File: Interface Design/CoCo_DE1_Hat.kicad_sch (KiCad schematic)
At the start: 24 parts, among them J1 J1, J2 J2, J3 J3, J4 J4, J5 J5, J6 J6, U1 74LVC245A, U2 74LVC245A, U3 74LVC245A, U4 74LVC245A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

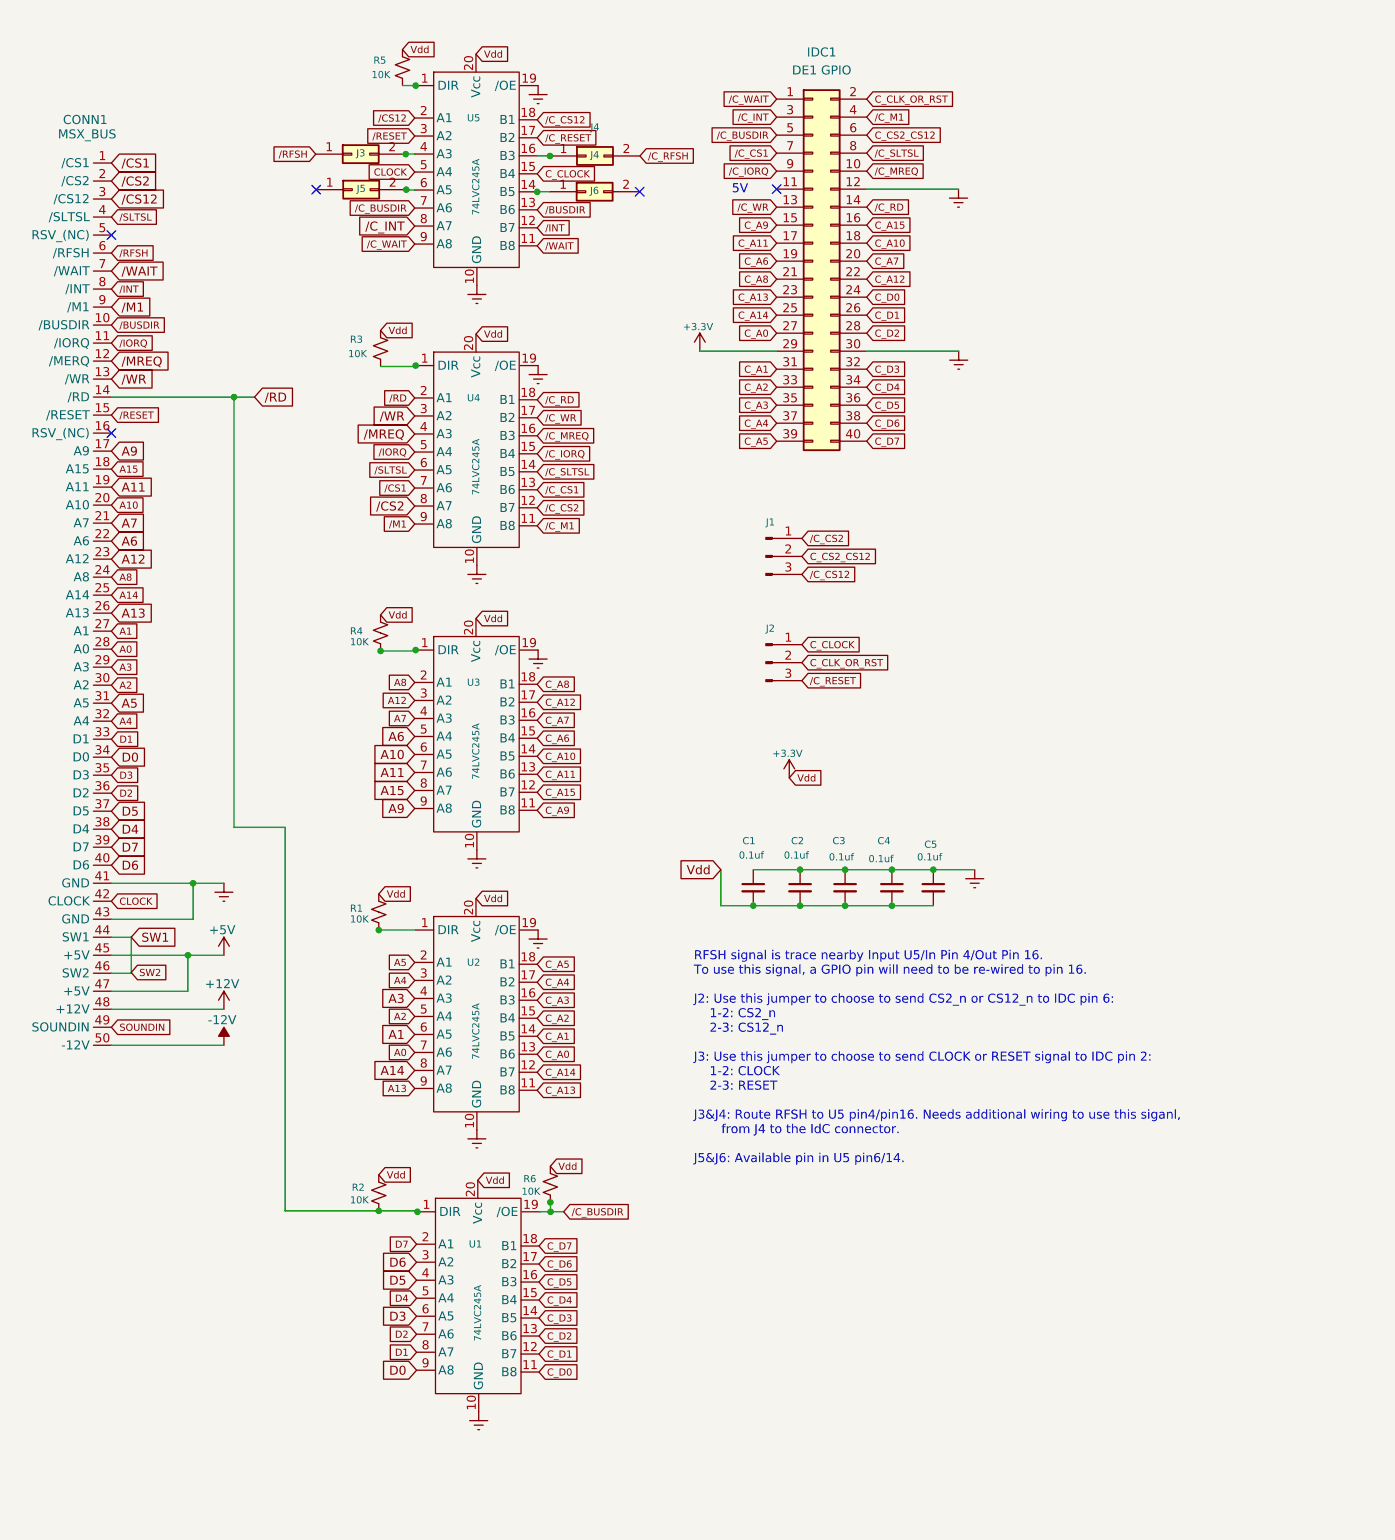
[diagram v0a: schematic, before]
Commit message: Adding PCB layout
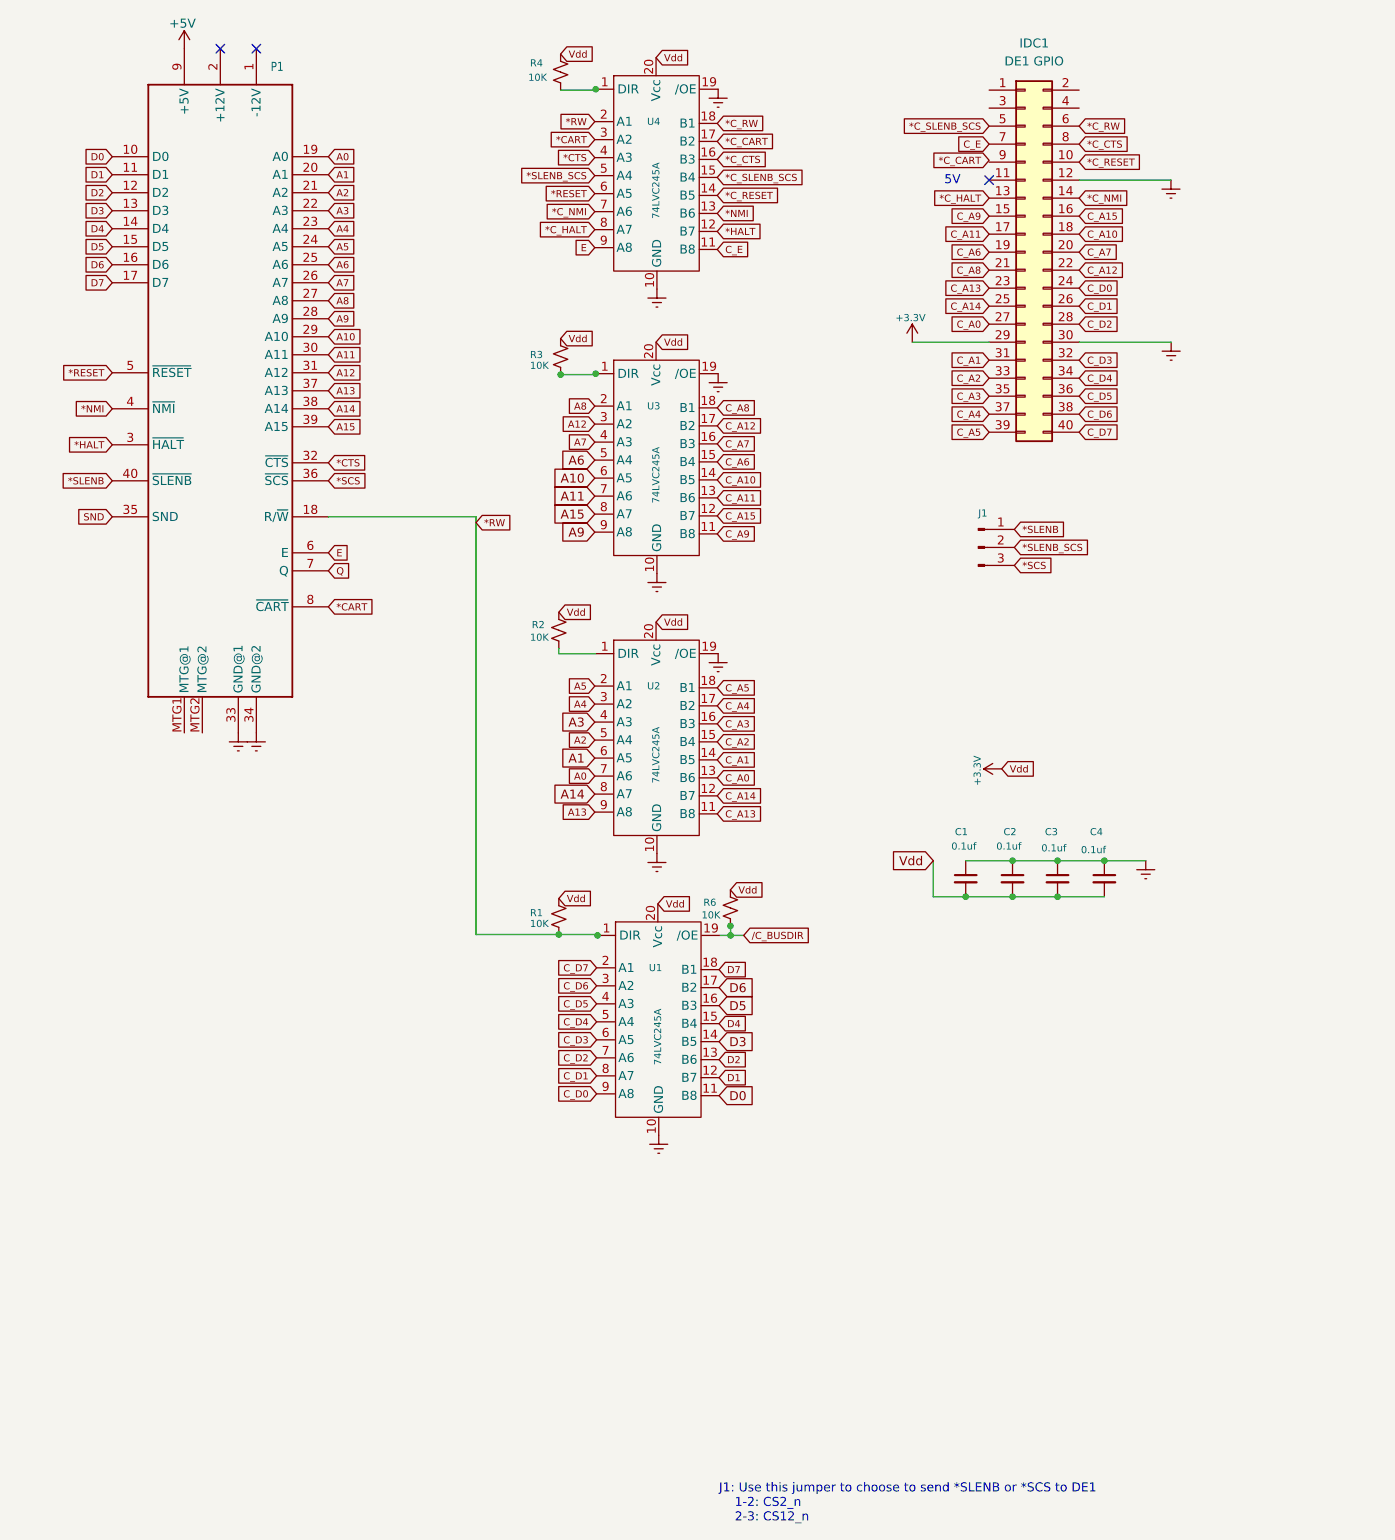
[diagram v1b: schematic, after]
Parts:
- removed C5: 0.1uf, Capacitor_THT:C_Disc_D3.0mm_W1.6mm_P2.50mm, symbol Device:C_Small
- removed CONN1: MSX_BUS, Roni Footprints:MSX_CART, symbol Roni:MSX_BUS
- removed J2: J2, Connector_PinHeader_2.54mm:PinHeader_1x03_P2.54mm_Vertical, symbol Connector:Conn_01x03_Male
- removed J3: J3, Connector_PinHeader_2.54mm:PinHeader_1x02_P2.54mm_Vertical, symbol Connector_Generic:Conn_02x01
- removed J4: J4, Connector_PinHeader_2.54mm:PinHeader_1x02_P2.54mm_Vertical, symbol Connector_Generic:Conn_02x01
- removed J5: J5, Connector_PinHeader_2.54mm:PinHeader_1x02_P2.54mm_Vertical, symbol Connector_Generic:Conn_02x01
- removed J6: J6, Connector_PinHeader_2.54mm:PinHeader_1x02_P2.54mm_Vertical, symbol Connector_Generic:Conn_02x01
- removed R5: 10K, Resistor_THT:R_Axial_DIN0207_L6.3mm_D2.5mm_P7.62mm_Horizontal, symbol Device:R_Small_US
- removed U5: 74LVC245A, Package_DIP:DIP-20_W7.62mm, symbol Roni:74LVC245A
- added P1: CoCo_Slot, Roni Footprints:COCO-CART-HAT, symbol Roni Symbols:CoCo_Slot
- IDC1: footprint Connector_IDC:IDC-Header_2x20_P2.54mm_Vertical -> Connector_PinHeader_2.54mm:PinHeader_2x20_P2.54mm_Vertical
- R1, R2, R6: footprint Resistor_THT:R_Axial_DIN0207_L6.3mm_D2.5mm_P7.62mm_Horizontal -> Resistor_THT:R_Axial_DIN0204_L3.6mm_D1.6mm_P5.08mm_Horizontal
- R3: renamed from R4; footprint Resistor_THT:R_Axial_DIN0207_L6.3mm_D2.5mm_P7.62mm_Horizontal -> Resistor_THT:R_Axial_DIN0204_L3.6mm_D1.6mm_P5.08mm_Horizontal
- R4: renamed from R3; footprint Resistor_THT:R_Axial_DIN0207_L6.3mm_D2.5mm_P7.62mm_Horizontal -> Resistor_THT:R_Axial_DIN0204_L3.6mm_D1.6mm_P5.08mm_Horizontal
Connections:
- net +5V: now also P1.9 (+5V)
- net A0: now also P1.19 (A0)
- net A1: now also P1.20 (A1)
- net A10: now also P1.29 (A10)
- net A11: now also P1.30 (A11)
- net A12: now also P1.31 (A12)
- net A13: now also P1.37 (A13)
- net A14: now also P1.38 (A14)
- net A15: now also P1.39 (A15)
- net A2: now also P1.21 (A2)
- net A3: now also P1.22 (A3)
- net A4: now also P1.23 (A4)
- net A5: now also P1.24 (A5)
- net A6: now also P1.25 (A6)
- net A7: now also P1.26 (A7)
- net A8: now also P1.27 (A8)
- net A9: now also P1.28 (A9)
- net C_D0: now also U1.9 (A8); no longer U1.11 (B8)
- net C_D1: now also U1.8 (A7); no longer U1.12 (B7)
- net C_D2: now also U1.7 (A6); no longer U1.13 (B6)
- net C_D3: now also U1.6 (A5); no longer U1.14 (B5)
- net C_D4: now also U1.5 (A4); no longer U1.15 (B4)
- net C_D5: now also U1.4 (A3); no longer U1.16 (B3)
- net C_D6: now also U1.3 (A2); no longer U1.17 (B2)
- net C_D7: now also U1.2 (A1); no longer U1.18 (B1)
- net D0: now also U1.11 (B8), P1.10 (D0); no longer U1.9 (A8)
- net D1: now also U1.12 (B7), P1.11 (D1); no longer U1.8 (A7)
- net D2: now also U1.13 (B6), P1.12 (D2); no longer U1.7 (A6)
- net D3: now also U1.14 (B5), P1.13 (D3); no longer U1.6 (A5)
- net D4: now also U1.15 (B4), P1.14 (D4); no longer U1.5 (A4)
- net D5: now also U1.16 (B3), P1.15 (D5); no longer U1.4 (A3)
- net D6: now also U1.17 (B2), P1.16 (D6); no longer U1.3 (A2)
- net D7: now also U1.18 (B1), P1.17 (D7); no longer U1.2 (A1)
- net GNDREF: now also P1.33 (GND@1), P1.34 (GND@2)
- net /C_BUSDIR: no longer IDC1.5 (Pin_5)
- net at U2.1 (DIR): now also R2.2; no longer R1.2
- net C_CLK_OR_RST: no longer names the net of IDC1.2 (Pin_2)
- net C_CS2_CS12 renamed *C_RW
- net *C_RW: now also U4.18 (B1); no longer J1.2 (Pin_2)
- net /CS1 renamed *C_NMI
- net *C_NMI: now also IDC1.14 (Pin_14)
- net /CS2 renamed *C_HALT
- net *C_HALT: now also IDC1.13 (Pin_13)
- net /C_CS1 renamed *NMI
- net *NMI: now also P1.4 (~{NMI}); no longer IDC1.7 (Pin_7)
- net /C_CS12 renamed *SCS
- net *SCS: now also P1.36 (~{SCS})
- net /C_CS2 renamed *HALT
- net *HALT: now also P1.3 (~{HALT}); no longer J1.1 (Pin_1)
- net /C_INT: no longer names the net of IDC1.3 (Pin_3)
- net /C_IORQ: no longer names the net of IDC1.9 (Pin_9)
- net /C_IORQ: no longer U4.15 (B4)
- net /C_M1: no longer names the net of IDC1.4 (Pin_4)
- net /C_M1: no longer U4.11 (B8)
- net /C_MREQ renamed *C_CTS
- net *C_CTS: now also IDC1.8 (Pin_8); no longer IDC1.10 (Pin_10)
- removed net /C_RD: IDC1.14 (Pin_14), U4.18 (B1)
- net /C_SLTSL renamed *C_RESET
- net *C_RESET: now also IDC1.10 (Pin_10); no longer IDC1.8 (Pin_8)
- net /C_WAIT: no longer names the net of IDC1.1 (Pin_1)
- net /C_WR renamed *C_CART
- net *C_CART: no longer IDC1.13 (Pin_13)
- net /IORQ renamed *SLENB_SCS
- net *SLENB_SCS: now also J1.2 (Pin_2)
- net /M1 renamed E
- net E: now also P1.6 (E)
- net /MREQ renamed *CTS
- net *CTS: now also P1.32 (~{CTS})
- net /RD renamed *RW
- net *RW: now also R1.2, P1.18 (R/~{W}); no longer R2.2
- net /SLTSL renamed *RESET
- net *RESET: now also P1.5 (~{RESET})
- net /WR renamed *CART
- net *CART: now also P1.8 (~{CART})
- new net *C_SLENB_SCS: IDC1.5 (Pin_5), U4.15 (B4)
- new net *SLENB: J1.1 (Pin_1), P1.40 (~{SLENB})
- new net C_E: IDC1.7 (Pin_7), U4.11 (B8)
- new net Q: P1.7 (Q)
- new net SND: P1.35 (SND)
- no-connect marks 5 -> 3
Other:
- note added: "J1: Use this jumper to choose to send *SLENB or *SCS to DE1 1-2: CS2_n 2-3: CS12_n"
- note removed: "RFSH signal is trace nearby Input U5/In Pin 4/Out Pin 16. To use this signal, a GPIO pin will need to be re-wired to pin 16. J2: Use this jumper to choose to send CS2_n or CS12_n to IDC pin 6: 1-2: CS2_n 2-3: CS12_n J3: Use this jumper to choose to send CLOCK or RESET signal to IDC pin 2: 1-2: CLOCK 2-3: RESET J3&J4: Route RFSH to U5 pin4/pin16. Needs additional wiring to use this siganl, from J4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"
- moved on the sheet: C1, C2, C3, C4, IDC1, J1, R1, R2, R3, R4, R6, U1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

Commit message: Project completd
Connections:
- net *CART: now also U4.14 (B5); no longer U4.3 (A2)
- net *CTS: now also U3.7 (A6); no longer U4.4 (A3)
- net *C_CART: now also IDC1.32 (Pin_32), U4.6 (A5); no longer U4.17 (B2)
- net *C_CTS: now also IDC1.5 (Pin_5), U3.13 (B6); no longer IDC1.8 (Pin_8), U4.16 (B3)
- net *C_HALT: now also IDC1.31 (Pin_31), U4.5 (A4); no longer IDC1.13 (Pin_13), U4.8 (A7)
- net *C_RESET: now also IDC1.36 (Pin_36), U4.17 (B2); no longer IDC1.10 (Pin_10), U4.14 (B5)
- net *C_RW: now also IDC1.34 (Pin_34), U4.16 (B3); no longer IDC1.6 (Pin_6), U4.18 (B1)
- net *HALT: now also U4.15 (B4); no longer U4.12 (B7)
- net *NMI: now also J1.3 (Pin_3); no longer U4.13 (B6)
- net *RESET: now also U4.3 (A2); no longer U4.6 (A5)
- net *RW: now also U4.4 (A3); no longer P1.18 (R/~{W}), R1.2, U1.1 (DIR), U4.2 (A1)
- net *SCS: now also U3.8 (A7); no longer J1.3 (Pin_3)
- net A0: now also U4.9 (A8); no longer U2.7 (A6)
- net A1: now also U4.8 (A7); no longer U2.6 (A5)
- net A10: now also U2.6 (A5); no longer U3.6 (A5)
- net A11: now also U3.6 (A5); no longer U3.7 (A6)
- net A12: now also U2.7 (A6); no longer U3.3 (A2)
- net A13: now also U2.8 (A7); no longer U2.9 (A8)
- net A14: now also U3.9 (A8); no longer U2.8 (A7)
- net A15: now also U2.9 (A8); no longer U3.8 (A7)
- net A2: now also U2.2 (A1); no longer U2.5 (A4)
- net A3: now also U3.2 (A1); no longer U2.4 (A3)
- net A5: now also U3.3 (A2); no longer U2.2 (A1)
- net A6: now also U2.4 (A3); no longer U3.5 (A4)
- net A8: now also U2.5 (A4); no longer U3.2 (A1)
- net A9: now also U3.5 (A4); no longer U3.9 (A8)
- net C_A0: now also IDC1.21 (Pin_21), U4.11 (B8); no longer IDC1.27 (Pin_27), U2.13 (B6)
- net C_A1: now also IDC1.23 (Pin_23), U4.12 (B7); no longer IDC1.31 (Pin_31), U2.14 (B5)
- net C_A10: now also IDC1.17 (Pin_17), U2.14 (B5); no longer IDC1.18 (Pin_18), U3.14 (B5)
- net C_A11: now also IDC1.6 (Pin_6), U3.14 (B5); no longer IDC1.17 (Pin_17), U3.13 (B6)
- net C_A12: now also IDC1.18 (Pin_18), U2.13 (B6); no longer IDC1.22 (Pin_22), U3.17 (B2)
- net C_A13: now also IDC1.4 (Pin_4), U2.12 (B7); no longer IDC1.23 (Pin_23), U2.11 (B8)
- net C_A14: now also IDC1.1 (Pin_1), U3.11 (B8); no longer IDC1.25 (Pin_25), U2.12 (B7)
- net C_A15: now also IDC1.2 (Pin_2), U2.11 (B8); no longer IDC1.16 (Pin_16), U3.12 (B7)
- net C_A2: now also IDC1.24 (Pin_24), U2.18 (B1); no longer IDC1.33 (Pin_33), U2.15 (B4)
- net C_A3: now also IDC1.9 (Pin_9), U3.18 (B1); no longer IDC1.35 (Pin_35), U2.16 (B3)
- net C_A4: now also IDC1.22 (Pin_22); no longer IDC1.37 (Pin_37)
- net C_A5: now also IDC1.10 (Pin_10), U3.17 (B2); no longer IDC1.39 (Pin_39), U2.18 (B1)
- net C_A6: now also U2.16 (B3); no longer U3.15 (B4)
- net C_A7: now also IDC1.8 (Pin_8); no longer IDC1.20 (Pin_20)
- net C_A8: now also IDC1.20 (Pin_20), U2.15 (B4); no longer IDC1.21 (Pin_21), U3.18 (B1)
- net C_A9: now also IDC1.7 (Pin_7), U3.15 (B4); no longer IDC1.15 (Pin_15), U3.11 (B8)
- net C_D0: now also IDC1.40 (Pin_40), U1.2 (A1); no longer IDC1.24 (Pin_24), U1.9 (A8)
- net C_D1: now also IDC1.39 (Pin_39), U1.3 (A2); no longer IDC1.26 (Pin_26), U1.8 (A7)
- net C_D2: now also IDC1.37 (Pin_37), U1.4 (A3); no longer IDC1.28 (Pin_28), U1.7 (A6)
- net C_D3: now also IDC1.35 (Pin_35), U1.5 (A4); no longer IDC1.32 (Pin_32), U1.6 (A5)
- net C_D4: now also IDC1.33 (Pin_33), U1.6 (A5); no longer IDC1.34 (Pin_34), U1.5 (A4)
- net C_D5: now also IDC1.27 (Pin_27), U1.7 (A6); no longer IDC1.36 (Pin_36), U1.4 (A3)
- net C_D6: now also IDC1.28 (Pin_28), U1.8 (A7); no longer IDC1.38 (Pin_38), U1.3 (A2)
- net C_D7: now also IDC1.26 (Pin_26), U1.9 (A8); no longer IDC1.40 (Pin_40), U1.2 (A1)
- net D0: now also U1.18 (B1); no longer U1.11 (B8)
- net D1: now also U1.17 (B2); no longer U1.12 (B7)
- net D2: now also U1.16 (B3); no longer U1.13 (B6)
- net D3: now also U1.15 (B4); no longer U1.14 (B5)
- net D4: now also U1.14 (B5); no longer U1.15 (B4)
- net D5: now also U1.13 (B6); no longer U1.16 (B3)
- net D6: now also U1.12 (B7); no longer U1.17 (B2)
- net D7: now also U1.11 (B8); no longer U1.18 (B1)
- net Q: now also U4.7 (A6)
- net /C_BUSDIR: now also IDC1.15 (Pin_15)
- net *C_SCS: now reaches IDC1.3 (Pin_3)
- net *C_SCS: now also U3.12 (B7)
- net *C_NMI: no longer names the net of IDC1.14 (Pin_14)
- net *C_NMI: no longer U4.7 (A6)
- removed net *C_SLENB_SCS: IDC1.5 (Pin_5), U4.15 (B4)
- net *SLENB_SCS renamed *NMI_SLENB
- net *NMI_SLENB: now also U4.18 (B1); no longer U4.5 (A4)
- removed net C_E: IDC1.7 (Pin_7), U4.11 (B8)
- net E: no longer names the net of P1.6 (E)
- net E: no longer U4.9 (A8)
- net SND: no longer names the net of P1.35 (SND)
- new net: P1.18 (R/~{W}), R1.2, U1.1 (DIR)
- new net *C_NMI_SLENB: IDC1.38 (Pin_38), U4.2 (A1)
- new net C_Q: IDC1.25 (Pin_25), U4.13 (B6)
- no-connect marks 3 -> 5
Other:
- note added: "J1: Use this jumper to choose to send *SLENB or *SCS to DE1 1-2: *SLENB 2-3: *NMI"
- note removed: "J1: Use this jumper to choose to send *SLENB or *SCS to DE1 1-2: CS2_n 2-3: CS12_n"
- title: MSX DE1 Hat -> CoCo DE1 Hat
- moved on the sheet: C1, C2, C3, C4, J1
